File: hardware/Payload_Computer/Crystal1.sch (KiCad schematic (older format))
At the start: 3 parts, among them Y1 Crystal_GND24

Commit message: Minor Library Changes
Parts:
- Y1: symbol Payload_Computer-rescue:Crystal_GND24-Symbols -> Symbols:Crystal_GND24
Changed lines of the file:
@@
 $Descr A4 11693 8268
 encoding utf-8
-Sheet 3 21
+Sheet 3 24
 Title ""
 Date ""
@@
 $EndDescr
 $Comp
-L Payload_Computer-rescue:Crystal_GND24-Symbols Y1
+L Symbols:Crystal_GND24 Y1
 U 1 1 5F84C384
 P 6150 3500

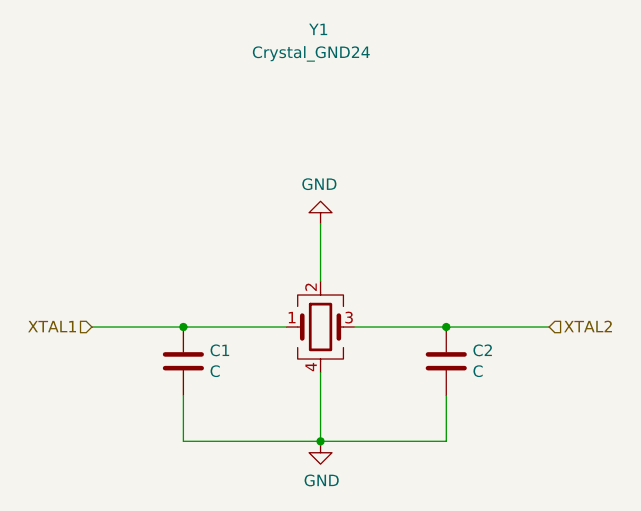
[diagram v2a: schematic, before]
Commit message: Updated processor for arduino. Fixed schematic a bit
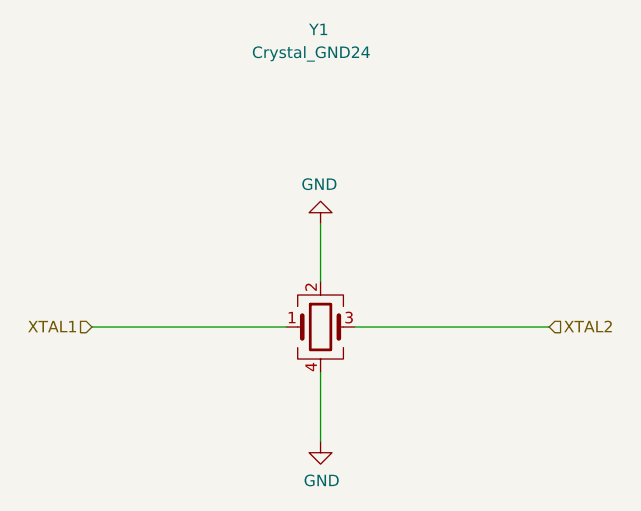
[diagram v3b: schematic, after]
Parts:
- removed C1, C2: C, symbol Device:C
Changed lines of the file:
@@
 $Descr A4 11693 8268
 encoding utf-8
-Sheet 3 27
+Sheet 2 26
 Title ""
 Date ""
@@
 	-1   0    0    1
 $EndComp
-$Comp
-L Device:C C2
-U 1 1 5F84D9F5
-P 6700 3650
-F 0 "C2" H 6815 3696 50  0000 L CNN
-F 1 "C" H 6815 3605 50  0000 L CNN
-F 2 "" H 6738 3500 50  0001 C CNN
-F 3 "~" H 6700 3650 50  0001 C CNN
-	1    6700 3650
-	1    0    0    -1
-$EndComp
-$Comp
-L Device:C C1
-U 1 1 5F84E009
-P 5550 3650
-F 0 "C1" H 5665 3696 50  0000 L CNN
-F 1 "C" H 5665 3605 50  0000 L CNN
-F 2 "" H 5588 3500 50  0001 C CNN
-F 3 "~" H 5550 3650 50  0001 C CNN
-	1    5550 3650
-	1    0    0    -1
-$EndComp
-Wire Wire Line
-	6300 3500 6700 3500
-Wire Wire Line
-	6000 3500 5550 3500
-Wire Wire Line
-	5550 3800 5550 4000
 Wire Wire Line
 	6150 3700 6150 4000
-Connection ~ 6150 4000
-Wire Wire Line
-	5550 4000 6150 4000
-Wire Wire Line
-	6700 3800 6700 4000
-Wire Wire Line
-	6700 4000 6150 4000
 Text HLabel 7150 3500 2    50   Input ~ 0
 XTAL2
@@
 XTAL1
 Wire Wire Line
-	6700 3500 7150 3500
-Connection ~ 6700 3500
+	6150 3300 6150 3050
 Wire Wire Line
-	5550 3500 5150 3500
-Connection ~ 5550 3500
+	5150 3500 6000 3500
 Wire Wire Line
-	6150 3300 6150 3050
+	6300 3500 7150 3500
 $EndSCHEMATC

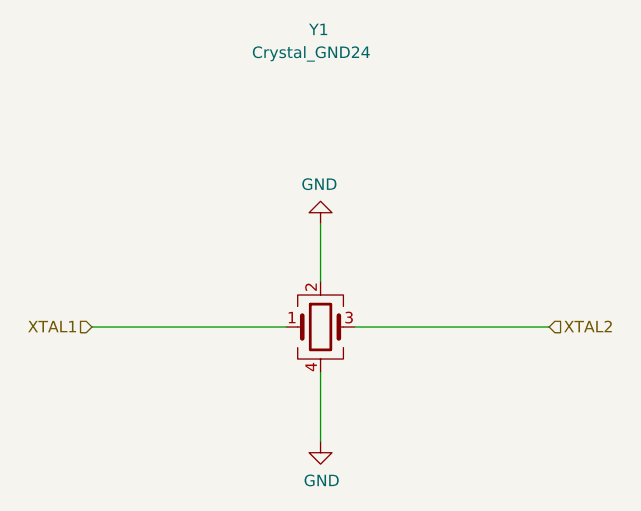
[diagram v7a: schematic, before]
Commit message: Added last footprints and started routing
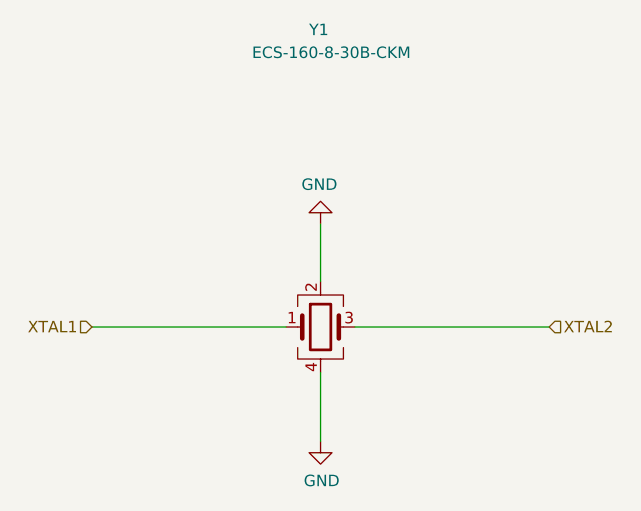
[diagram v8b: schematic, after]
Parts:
- Y1: value Crystal_GND24 -> ECS-160-8-30B-CKM; footprint (none) -> LED:16Mhz
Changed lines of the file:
@@
 P 6150 3500
 F 0 "Y1" H 6100 4800 50  0000 L CNN
-F 1 "Crystal_GND24" H 5850 4700 50  0000 L CNN
-F 2 "" H 6150 3500 50  0001 C CNN
+F 1 "ECS-160-8-30B-CKM" H 5850 4700 50  0000 L CNN
+F 2 "LED:16Mhz" H 6150 3500 50  0001 C CNN
 F 3 "~" H 6150 3500 50  0001 C CNN
 	1    6150 3500
